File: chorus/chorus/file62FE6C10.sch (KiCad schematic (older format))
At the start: 7 parts, among them U4 MN3102, U7 MN3207

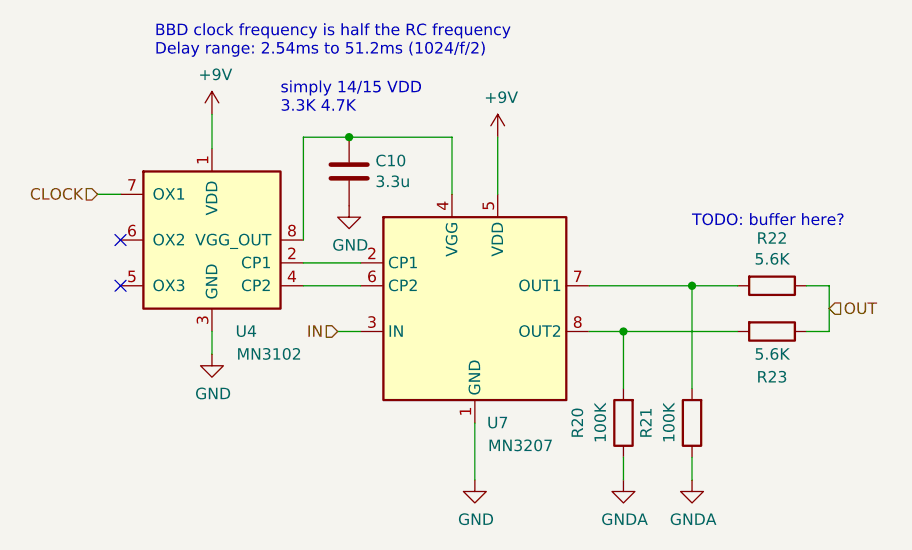
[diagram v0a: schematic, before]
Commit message: add wet/dry mix and recalculate filters
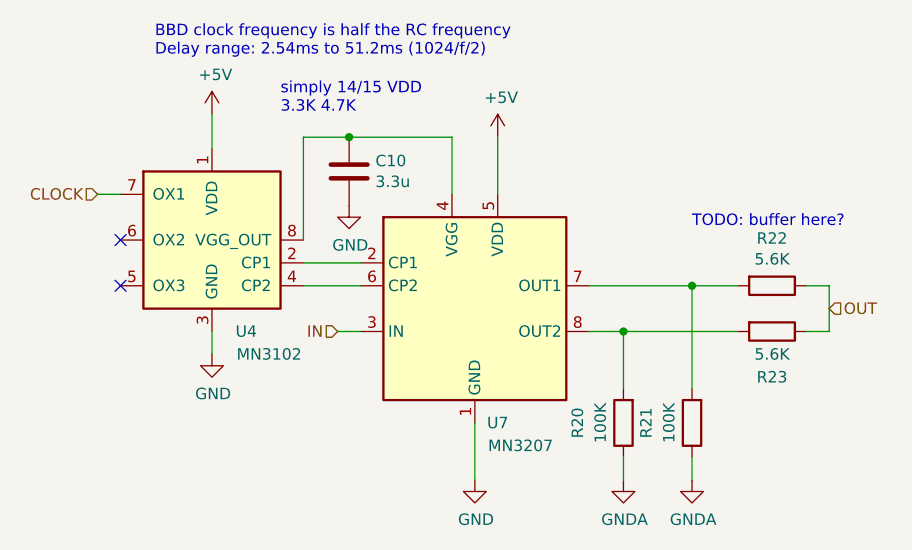
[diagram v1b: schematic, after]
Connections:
- net +9V renamed +5V
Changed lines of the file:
@@
 $Descr A4 11693 8268
 encoding utf-8
-Sheet 5 6
+Sheet 4 6
 Title ""
 Date ""
@@
 NoConn ~ 4100 3400
 NoConn ~ 4100 3200
-$Comp
-L power:+9V #PWR?
-U 1 1 62FF72F4
-P 4500 2650
-AR Path="/62FF72F4" Ref="#PWR?"  Part="1"
-AR Path="/62FE6C11/62FF72F4" Ref="#PWR0139"  Part="1"
-F 0 "#PWR0139" H 4500 2500 50  0001 C CNN
-F 1 "+9V" H 4515 2823 50  0000 C CNN
-F 2 "" H 4500 2650 50  0001 C CNN
-F 3 "" H 4500 2650 50  0001 C CNN
-	1    4500 2650
-	1    0    0    -1
-$EndComp
 Text Notes 4800 2650 0    50   ~ 0
 simply 14/15 VDD\n3.3K 4.7K
@@
 Wire Wire Line
 	4500 2800 4500 2650
-$Comp
-L power:+9V #PWR?
-U 1 1 62FF731F
-P 5750 2750
-AR Path="/62FF731F" Ref="#PWR?"  Part="1"
-AR Path="/62FE6C11/62FF731F" Ref="#PWR0141"  Part="1"
-F 0 "#PWR0141" H 5750 2600 50  0001 C CNN
-F 1 "+9V" H 5765 2923 50  0000 C CNN
-F 2 "" H 5750 2750 50  0001 C CNN
-F 3 "" H 5750 2750 50  0001 C CNN
-	1    5750 2750
-	1    0    0    -1
-$EndComp
 Wire Wire Line
 	4500 3700 4500 3600
@@
 Text HLabel 7200 3500 2    50   Input ~ 0
 OUT
+$Comp
+L power:+5V #PWR?
+U 1 1 62C8354C
+P 4500 2650
+AR Path="/62C8354C" Ref="#PWR?"  Part="1"
+AR Path="/62FE6C11/62C8354C" Ref="#PWR?"  Part="1"
+F 0 "#PWR?" H 4500 2500 50  0001 C CNN
+F 1 "+5V" H 4515 2823 50  0000 C CNN
+F 2 "" H 4500 2650 50  0001 C CNN
+F 3 "" H 4500 2650 50  0001 C CNN
+	1    4500 2650
+	1    0    0    -1
+$EndComp
+$Comp
+L power:+5V #PWR?
+U 1 1 62C8403F
+P 5750 2750
+AR Path="/62C8403F" Ref="#PWR?"  Part="1"
+AR Path="/62FE6C11/62C8403F" Ref="#PWR?"  Part="1"
+F 0 "#PWR?" H 5750 2600 50  0001 C CNN
+F 1 "+5V" H 5765 2923 50  0000 C CNN
+F 2 "" H 5750 2750 50  0001 C CNN
+F 3 "" H 5750 2750 50  0001 C CNN
+	1    5750 2750
+	1    0    0    -1
+$EndComp
 $EndSCHEMATC
